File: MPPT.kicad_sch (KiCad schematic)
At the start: 95 parts

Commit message: schematic and layout revision.
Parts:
- removed C? (x2): 100uF, Capacitor_SMD:C_1210_3225Metric, symbol Device:C
- removed C?: 47uF, Capacitor_SMD:C_1206_3216Metric, symbol Device:C
- removed C?: 10uF, Capacitor_SMD:C_0805_2012Metric, symbol Device:C_Small
- removed C? (x2): 100nF, Capacitor_SMD:C_0805_2012Metric, symbol Device:C_Small
- removed D? (x3): 3.9V Zener, Diode_SMD:D_SOD-123F, symbol Device:D_Zener_Small
- removed D?: Diode, Diode_SMD:D_SOD-123F, symbol Device:D_Small
- removed L?: 6.8uH, Inductor_SMD:L_Taiyo-Yuden_NR-50xx, symbol Device:L_Small
- removed LED?: Tracking (Blue), LED_SMD:LED_0805_2012Metric, symbol Device:LED_Small
- removed LED?: Array Live (Green), LED_SMD:LED_0805_2012Metric, symbol Device:LED_Small
- removed LED?: Battery Live (Green), LED_SMD:LED_0805_2012Metric, symbol Device:LED_Small
- removed LED?: PWM (Blue), LED_SMD:LED_0805_2012Metric, symbol Device:LED_Small
- removed LED?: Car 12V (Green), LED_SMD:LED_0805_2012Metric, symbol Device:LED_Small
- removed LED?: Device 9V (Green), LED_SMD:LED_0805_2012Metric, symbol Device:LED_Small
- removed LED?: CAN_Tx (Blue), LED_SMD:LED_0805_2012Metric, symbol Device:LED_Small
- removed LED?: CAN_Rx (Blue), LED_SMD:LED_0805_2012Metric, symbol Device:LED_Small
- removed LED?: BPS Full (Blue), LED_SMD:LED_0805_2012Metric, symbol Device:LED_Small
- removed LED?: Error (Amber), LED_SMD:LED_0805_2012Metric, symbol Device:LED_Small
- removed R? (x2): 2k, Resistor_SMD:R_0805_2012Metric, symbol Device:R
- removed R? (x2): 1k, Resistor_SMD:R_0805_2012Metric, symbol Device:R
- removed R? (x6): 330, Resistor_SMD:R_0805_2012Metric, symbol Device:R
- removed R?: 15k, Resistor_SMD:R_0805_2012Metric, symbol Device:R
- removed R? (x2): 100k, Resistor_SMD:R_0805_2012Metric, symbol Device:R
- removed R?: 27k, Resistor_SMD:R_0805_2012Metric, symbol Device:R
- removed TP?: Arr_V, TestPoint:TestPoint_Pad_1.0x1.0mm, symbol Connector:TestPoint
- removed TP?: -ARR, TestPoint:TestPoint_Pad_1.0x1.0mm, symbol Connector:TestPoint
- removed TP?: +ARR, TestPoint:TestPoint_Pad_1.0x1.0mm, symbol Connector:TestPoint
- removed TP?: +BATT, TestPoint:TestPoint_Pad_1.0x1.0mm, symbol Connector:TestPoint
- removed TP?: -BATT, TestPoint:TestPoint_Pad_1.0x1.0mm, symbol Connector:TestPoint
- removed TP?: Board GND, TestPoint:TestPoint_Pad_1.0x1.0mm, symbol Connector:TestPoint
- removed TP?: Batt_V, TestPoint:TestPoint_Pad_1.0x1.0mm, symbol Connector:TestPoint
- removed TP?: Car GND, TestPoint:TestPoint_Pad_1.0x1.0mm, symbol Connector:TestPoint
- removed TP?: 12V, TestPoint:TestPoint_Pad_1.0x1.0mm, symbol Connector:TestPoint
- removed TP?: +5V, TestPoint:TestPoint_Pad_1.0x1.0mm, symbol Connector:TestPoint
- removed U?: PQMC3-D12-S9-S, MPPT-PrimaryPCB:490_PQMC3_D12_S12_S, symbol Array:PWR_REG_PQMC3-Dx-Sx-S
- removed U? (x2): MAX40075, Package_TO_SOT_SMD:SOT-23-6, symbol Amplifier_Operational:MAX4238AUT
- added C1, C14, C19, C2: 10uF, Capacitor_SMD:C_0805_2012Metric, symbol Device:C_Small
- added C10, C11, C12, C13, C15, C16, C20: 100nF, Capacitor_SMD:C_0805_2012Metric, symbol Device:C_Small
- added C17, C21: 10nF, Capacitor_SMD:C_0805_2012Metric, symbol Device:C_Small
- added C18: 220nF, Capacitor_SMD:C_0805_2012Metric, symbol Device:C_Small
- added D1: 13.2V, Diode_SMD:D_SOD-323F, symbol Device:D_Zener_Small
- added D10, D2, D7, D8, D9: 3.3V Zener, Diode_SMD:D_MiniMELF, symbol Device:D_Zener_Small
- added J5: CAN_In, Connector_Molex:Molex_Micro-Fit_3.0_43650-0415_1x04_P3.00mm_Vertical, symbol MPPT:CAN_Connector_43650-0427
- added J6: CAN_Out, Connector_Molex:Molex_Micro-Fit_3.0_43650-0415_1x04_P3.00mm_Vertical, symbol MPPT:CAN_Connector_43650-0427
- added JP1: Jumper, Connector_PinHeader_2.54mm:PinHeader_1x02_P2.54mm_Vertical, symbol Jumper:Jumper_2_Bridged
- added L3, L4: 1.8kOhm, Inductor_SMD:L_0805_2012Metric, symbol Device:FerriteBead_Small
- added LED1: 5V (Green), LED_SMD:LED_0805_2012Metric, symbol Device:LED_Small
- added LED10: Error (Amber), LED_SMD:LED_0805_2012Metric, symbol Device:LED
- added LED3, LED4: 9V (Green), LED_SMD:LED_0805_2012Metric, symbol Device:LED
- added LED5: Heartbeat (Blue), LED_SMD:LED_0805_2012Metric, symbol Device:LED
- added LED6: Tracking (Blue), LED_SMD:LED_0805_2012Metric, symbol Device:LED
- added LED7: PWM (Blue), LED_SMD:LED_0805_2012Metric, symbol Device:LED
- added LED8: CAN_Rx (Blue), LED_SMD:LED_0805_2012Metric, symbol Device:LED
- added LED9: CAN_Tx (Blue), LED_SMD:LED_0805_2012Metric, symbol Device:LED
- added R1: 330, Resistor_SMD:R_0805_2012Metric, symbol Device:R_Small
- added R10, R8: 100k, Resistor_SMD:R_0805_2012Metric, symbol Device:R
- added R11: 2k, Resistor_SMD:R_0805_2012Metric, symbol Device:R
- added R12: 0, Resistor_SMD:R_0805_2012Metric, symbol Device:R
- added R13, R14: 60.4, Resistor_SMD:R_0805_2012Metric, symbol Device:R_Small
- added R15: 15k, Resistor_SMD:R_0805_2012Metric, symbol Device:R
- added R16: 27k, Resistor_SMD:R_0805_2012Metric, symbol Device:R
- added R17, R18, R19, R20, R21, R22: 330, Resistor_SMD:R_0805_2012Metric, symbol Device:R
- added R6, R7: 2m, Resistor_SMD:R_1206_3216Metric, symbol Device:R
- added R9: 3k, Resistor_SMD:R_0805_2012Metric, symbol Device:R
- added TP1: 12V, TestPoint:TestPoint_Pad_1.0x1.0mm, symbol Connector:TestPoint
- added TP14, TP18: GND, TestPoint:TestPoint_Pad_1.0x1.0mm, symbol Connector:TestPoint
- added TP15: -ARR, TestPoint:TestPoint_Pad_1.0x1.0mm, symbol Connector:TestPoint
- added TP16: Array Current, TestPoint:TestPoint_Pad_1.0x1.0mm, symbol Connector:TestPoint
- added TP17: -BATT, TestPoint:TestPoint_Pad_1.0x1.0mm, symbol Connector:TestPoint
- added TP19: Battery Current, TestPoint:TestPoint_Pad_1.0x1.0mm, symbol Connector:TestPoint
- added TP2: Car GND, TestPoint:TestPoint_Pad_1.0x1.0mm, symbol Connector:TestPoint
- added TP20: +ARR, TestPoint:TestPoint_Pad_1.0x1.0mm, symbol Connector:TestPoint
- added TP21: Arr_V, TestPoint:TestPoint_Pad_1.0x1.0mm, symbol Connector:TestPoint
- added TP22: +BATT, TestPoint:TestPoint_Pad_1.0x1.0mm, symbol Connector:TestPoint
- added TP23: Batt_V, TestPoint:TestPoint_Pad_1.0x1.0mm, symbol Connector:TestPoint
- added TP24: CAN_Tx, TestPoint:TestPoint_Pad_1.0x1.0mm, symbol Connector:TestPoint
- added TP25: CAN_Rx, TestPoint:TestPoint_Pad_1.0x1.0mm, symbol Connector:TestPoint
- added TP26: CAN_ISO_Vout, TestPoint:TestPoint_Pad_1.0x1.0mm, symbol Connector:TestPoint
- added TP27: CAN_ISO_Vin, TestPoint:TestPoint_Pad_1.0x1.0mm, symbol Connector:TestPoint
- added TP28: CAN_ISO_GndIn, TestPoint:TestPoint_Pad_1.0x1.0mm, symbol Connector:TestPoint
- added TP29: CAN_ISO_GndOut, TestPoint:TestPoint_Pad_1.0x1.0mm, symbol Connector:TestPoint
- added TP3: +9V, TestPoint:TestPoint_Pad_1.0x1.0mm, symbol Connector:TestPoint
- added TP30: CAN_H, TestPoint:TestPoint_Pad_1.0x1.0mm, symbol Connector:TestPoint
- added TP31: CAN_L, TestPoint:TestPoint_Pad_1.0x1.0mm, symbol Connector:TestPoint
- added TP4: +3V3, TestPoint:TestPoint_Pad_1.0x1.0mm, symbol Connector:TestPoint
- added TP5: +5V, TestPoint:TestPoint_Pad_1.0x1.0mm, symbol Connector:TestPoint
- added TP6: Board GND, TestPoint:TestPoint_Pad_1.0x1.0mm, symbol Connector:TestPoint
- added U1: RI3-1205S, MPPT:CONV_RI3-1205S, symbol MPPT:RI3-1205S
- added U10: CDSOT23-T24CAN, Package_TO_SOT_SMD:SOT-23, symbol MPPT:CAN_Bus_Protector_CDSOT23-T24CAN
- added U5, U6: INA210, Package_DFN_QFN:UQFN-10_1.4x1.8mm_P0.4mm, symbol MPPT:OP_AMP_INA21x
- added U7, U8: MAX40075, Package_TO_SOT_SMD:SOT-23-6, symbol Amplifier_Operational:MAX4238AUT
- added U9: ADM3055E, MPPT:ADM3055EBRIZ, symbol MPPT:CAN_Chip_ADM3055E
- C3, C4: renamed from C?; Manufacturer Samsung Electro-Mechanics -> Samsung Elctro-Mechanics; Manufacturer Part Number (none) -> CL21B104KCFNNNE; Mouser Part (none) -> N/A; Part Number N/A -> (none); Projected Cost 0.0079 -> 0.0083
- C5: renamed from C?; Manufacturer Part Number (none) -> CL21B105KBFNNNE; Mouser Part (none) -> N/A; Part Number N/A -> (none)
- C6, C7: renamed from C?; Manufacturer Part Number (none) -> CL21A475KAQNNNE; Mouser Part (none) -> N/A; Part Number N/A -> (none)
- C8: renamed from C?; Manufacturer Part Number (none) -> 0805F225M500NT; Mouser Part (none) -> N/A; Part Number N/A -> (none)
- C9: renamed from C?; Alternative See 1nF, 2.2nF, 4.7nF, 10nF, 22nF, 47nF versions. -> (none); Alternative Part (none) -> See 1nF, 2.2nF, 4.7nF, 10nF, 22nF, 47nF versions.; Manufacturer Part Number (none) -> MKT1813247635; Mouser Part (none) -> 75-MKT1813247635; Part Number 75-MKT1813247635 -> (none)
- CP1, CP2: renamed from CP?; Manufacturer Part Number (none) -> SLPX102M250E5P3; Mouser Part (none) -> 598-SLPX102M250E5P3; Part Number 598-SLPX102M250E5P3 -> (none)
- D3: renamed from D?; Manufacturer Part Number (none) -> BZT52H-B16,115; Mouser Part (none) -> 771-BZT52HB16115; Part Number 771-BZT52HB16115 -> (none)
- D4, D5, D6: renamed from D?; Manufacturer Part Number (none) -> SCS308AHGC9; Mouser Part (none) -> 755-SCS308AHGC9; Part Number 755-SCS308AHGC9 -> (none)
- F1, F2: renamed from F?; footprint IV Curve Tracer:05200101Z_Fuze_Holder_5x20_PCB_Mount -> MPPT:05200101Z_Fuze_Holder_5x20_PCB_Mount; Manufacturer Part Number (none) -> 05200101Z; Mouser Part (none) -> 576-05200101Z; Part Number 576-05200101Z -> (none)
- HS1, HS2, HS3: renamed from HS?; Manufacturer Part Number (none) -> FA-T220-38E; Mouser Part (none) -> 588-FA-T220-38E; Part Number 588-FA-T220-38E -> (none)
- J1: renamed from J?; symbol Array:PWR_Connector_43650-0215 -> MPPT:PWR_Connector_43650-0215; Manufacturer Part Number (none) -> 43650-0215; Mouser Part (none) -> 538-43650-0215; Part Number 538-43650-0215 -> (none)
- J2: renamed from J?; Manufacturer Part Number (none) -> 43650-0215; Mouser Part (none) -> 538-43650-0215; Part Number 538-43650-0215 -> (none)
- J3, J4: renamed from J?; footprint IV Curve Tracer:PhoenixContact_PowerCombicon5_GF_2x7.62mm -> MPPT:PhoenixContact_PowerCombicon5_GF_2x7.62mm; symbol Array:PWR_Connector_1720796 -> MPPT:PWR_Connector_1720796; Manufacturer Part Number (none) -> 1720796; Mouser Part (none) -> 651-1720796; Part Number 651-1720796 -> (none)
- L1: renamed from L?; Manufacturer Part Number (none) -> NRS5040T6R8MMGJ; Mouser Part (none) -> 963-NRS5040T6R8MMGJ; Part Number 963-NRS5040T6R8MMGJ -> (none)
- L2: renamed from L?; footprint MPPT-PrimaryPCB:L_Toroid_Vertical_L46.0mm_W19.1mm_P21.80mm_Bourns_5700 -> MPPT:L_Toroid_Vertical_L46.0mm_W19.1mm_P21.80mm_Bourns_5700; Manufacturer Part Number (none) -> HF400-601M-8.0AV; Mouser Part (none) -> N/A; Part Number HF400-601M-8.0AV -> (none)
- LED2: renamed from LED?; Manufacturer Part Number (none) -> APTD2012LCGCK; Mouser Part (none) -> 604-APTD2012LCGCK; Part Number 604-APTD2012LCGCK -> (none)
- Q1, Q2: renamed from Q?; Alternative Part (none) -> https://www.mouser.com/ProductDetail/IXYS/IXTH62N65X2?qs=uw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; Manufacturer Toshiba -> IXYS; Manufacturer Part Number (none) -> IXFH80N65X2; Mouser Part (none) -> 747-IXFH80N65X2; Part Number 757-TK040N65ZS1F -> (none); Purchase Page https://www.mouser.com/ProductDetail/Toshiba/TK040N65ZS1F?q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 -> https://www.mouser.com/ProductDetail/IXYS/IXFH80N65X2?qs=gQ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
- R2: renamed from R?; Manufacturer Part Number (none) -> CRCW08051R50FKEAHP; Mouser Part (none) -> 71-CRCW08051R50FKEAH; Part Number 71-CRCW08051R50FKEAH -> (none)
- R3: renamed from R?; Manufacturer Part Number (none) -> 0805W8F3300T5E; Mouser Part (none) -> N/A; Part Number N/A -> (none)
- R4: renamed from R?; Manufacturer Part Number (none) -> 0805W8F1002T5E; Mouser Part (none) -> N/A; Part Number N/A -> (none)
- R5: renamed from R?; Alternative See 2, 10, 20, 33, 75, 150 ohm versions. -> (none); Alternative Part (none) -> See 2, 10, 20, 33, 75, 150 ohm versions.; Manufacturer Part Number (none) -> PWR220T-35-33R0J; Mouser Part (none) -> 652-PWR220T-35-33R0J; Part Number 652-PWR220T-35-33R0J -> (none)
- SW1: renamed from SW?; Manufacturer Part Number (none) -> TS02-66-50-BK-260-SCR-D; Mouser Part (none) -> 179-TS026650BK260SCR; Part Number 179-TS026650BK260SCR -> (none)
- SW2: renamed from SW?; footprint MPPT-PrimaryPCB:ADF02ST04_DIP_Switch_2_POS -> MPPT:ADF02ST04_DIP_Switch_2_POS; Manufacturer Part Number (none) -> ADF02ST04; Mouser Part (none) -> 506-ADF02ST04; Part Number 506-ADF02ST04 -> (none)
- U2: renamed from U?; footprint IV Curve Tracer:MODULE_NUCLEO-L432KC -> MPPT:MODULE_NUCLEO-L432KC; symbol Array:MCU_Nucleo_L432KC -> MPPT:MCU_Nucleo_L432KC; Manufacturer Part Number (none) -> 511-NUCLEO-L432KC; Mouser Part (none) -> 511-NUCLEO-L432KC; Part Number 511-NUCLEO-L432KC -> (none)
- U3: renamed from U?; symbol Array:UCC37321 -> MPPT:UCC37321; Manufacturer Part Number (none) -> UCC37321D; Mouser Part (none) -> N/A; Part Number UCC37321D -> (none)
- U4: renamed from U?; footprint IV Curve Tracer:IES01_PDS1 -> MPPT:IES01_PDS1; symbol Array:IES01_PDS1 -> MPPT:IES01_PDS1; Manufacturer Part Number (none) -> IES0105S09; Mouser Part (none) -> 209-IES0105S09; Part Number 209-IES0105S09 -> (none)
- gave numbers to parts that had none: 11
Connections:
- net +12V: now also C1.1, D1.1 (K), TP1.1, U1.2 (+VIN)
- net +3V3: now also C16.2, C17.1, TP4.1, U9.4 (V_IO)
- net +5V: now also C14.1, C15.2, C2.1, R1.1, TP5.1, U1.4 (+VOUT), U9.3 (V_In)
- net +9V: now also J2.1 (Pin_1), TP3.1; no longer J2.2 (Pin_2)
- net +9VA: now also C10.2, C11.2, C12.2, C13.2, U5.3 (V+), U6.3 (V+), U7.6 (V+), U8.6 (V+)
- net Array_Current: now also D7.1 (K), TP16.1, U5.6
- net Array_Voltage: now also D9.1 (K), TP21.1, U7.1, U7.4 (-)
- net Battery_Current: now also D8.1 (K), TP19.1, U6.6
- net Battery_Voltage: now also D10.1 (K), TP23.1, U8.1, U8.4 (-)
- net CAN_Rx: now also R20.1, TP25.1, U9.5 (RX)
- net CAN_Tx: now also R21.1, TP24.1, U9.7 (TX)
- net Error: now also R22.1
- net GND: now also J2.2 (Pin_2), C10.1, C11.1, C12.1, C13.1, C14.2, C15.1, C16.1, C17.2, C2.2, D10.2 (A), D2.2 (A), D7.2 (A), D8.2 (A), D9.2 (A), LED1.1 (K), LED10.1 (K), LED5.1 (K), LED6.1 (K), LED7.1 (K), LED8.1 (K), LED9.1 (K), R11.2, R6.2, R7.1, R9.2, TP14.1, TP18.1, TP6.1, U1.3 (-VOUT), U5.1 (REF), U5.2 (V-), U5.4 (+), U6.1 (REF), U6.2 (V-), U6.5 (-), U7.2 (V-), U7.5 (~{SHDN}), U8.2 (V-), U8.5 (~{SHDN}), U9.1 (GND_In), U9.10 (GND_In), U9.2 (GND_In); no longer J2.1 (Pin_1)
- net GNDPWR: now also C1.2, D1.2 (A), TP2.1, U1.1 (-VIN)
- net Heartbeat: now also R17.1
- net PWM: now also D2.1 (K), R19.1
- net Tracking: now also R18.1
- net +ARR: now reaches CP1.1, F1.1, L2.1
- net +ARR: now also R15.1, R8.2, TP20.1
- net +BATT: now reaches CP2.1, D5.1 (K), D6.1 (K), F2.2
- net +BATT: now also R10.2, R16.1, TP22.1
- net -Arr renamed -ARR
- net -ARR: now also LED3.1 (K), R6.1, TP15.1, U5.5 (-)
- net -Batt renamed -BATT
- net -BATT: now also LED4.1 (K), R7.2, TP17.1, U6.4 (+)
- net BPS_Full: no longer names the net of U2.12 (D9)
- new net: R8.1, R9.1, U7.3 (+)
- new net: LED1.2 (A), R1.2
- new net: C19.2, C20.1, C21.2, J5.2 (GND), J6.2 (GND), L4.1, R12.2, TP28.1, U10.3 (GND), U9.11 (GND_ISO_In), U9.15 (GND_ISO_In)
- new net: C18.2, L4.2, TP29.1, U9.18 (GND_ISO_Out), U9.20 (GND_ISO_Out)
- new net: LED4.2 (A), R16.2
- new net: LED5.2 (A), R17.2
- new net: R12.1, U9.12 (RS)
- new net: J5.4 (CAN_L), J6.4 (CAN_L), R14.2, TP31.1, U10.2 (CAN_L), U9.13 (CAN_L)
- new net: J5.3 (CAN_H), J6.3 (CAN_H), R13.1, TP30.1, U10.1 (CAN_H), U9.14 (CAN_H)
- new net: C19.1, C20.2, C21.1, J5.1 (5V), J6.1 (5V), L3.1, TP27.1, U9.16 (V_ISO_In)
- new net: C18.1, L3.2, TP26.1, U9.19 (V_ISO_Out)
- new net: LED8.2 (A), R20.2
- new net: LED3.2 (A), R15.2
- new net: LED9.2 (A), R21.2
- new net: R10.1, R11.1, U8.3 (+)
- new net: JP1.1 (A), R13.2
- new net: JP1.2 (B), R14.1
- new net: LED6.2 (A), R18.2
- new net: LED10.2 (A), R22.2
- new net: LED7.2 (A), R19.2
- no-connect marks 11 -> 15
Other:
- note added: "0-100V"
- note added: "0-150V"
- note added: "0-3V"
- note added: "0-6A"
- note added: "0-8A"
- note added: "7.5A 0-15mV"
- note added: "CAN"
- note added: "CAN Bus Protection"
- note added: "HIGH CURRENT FLOWS THROUGH THIS LOOP."
- note added: "Inputs: -10.8-13.2VDC (Car Power) -7-12VDC (External 9V Supply) -5VDC (Nucleo USB)"
- note added: "Must be close to V_ISO_In"
- note added: "Must be close to V_ISO_Out"
- note added: "Nucleo Connections"
- note added: "PWM Gate Driver"
- note added: "Powered and controlled by USB through STLink UART. Requires A7 (PA2) and A2 (PA3) to be reserved."
- note added: "VIN: 7-12V -> Input 5V0: 5V -> Output on USB/VIN 3V3: 3.3V -> Output always"
- note removed: "For decoupling, we add extra capacitors and unlink the power pins on either side."
- note removed: "GNDPWR"
- note removed: "High Power Control"
- note removed: "NOTE: We would ordinarily isolate the Nucleo from the high power regions, but we don't have a good way to do that without redesigning our sensors and our software. Therefore, for reasons of expediency, we're placing the Nucleo on the high power plane."
- note removed: "Note that A7 (PA2) and A2 (PA3) are reserved for STLink UART."
- moved on the sheet: C3, C4, C5, C6, C7, C8, C9, CP1, CP2, D3, D4, D5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

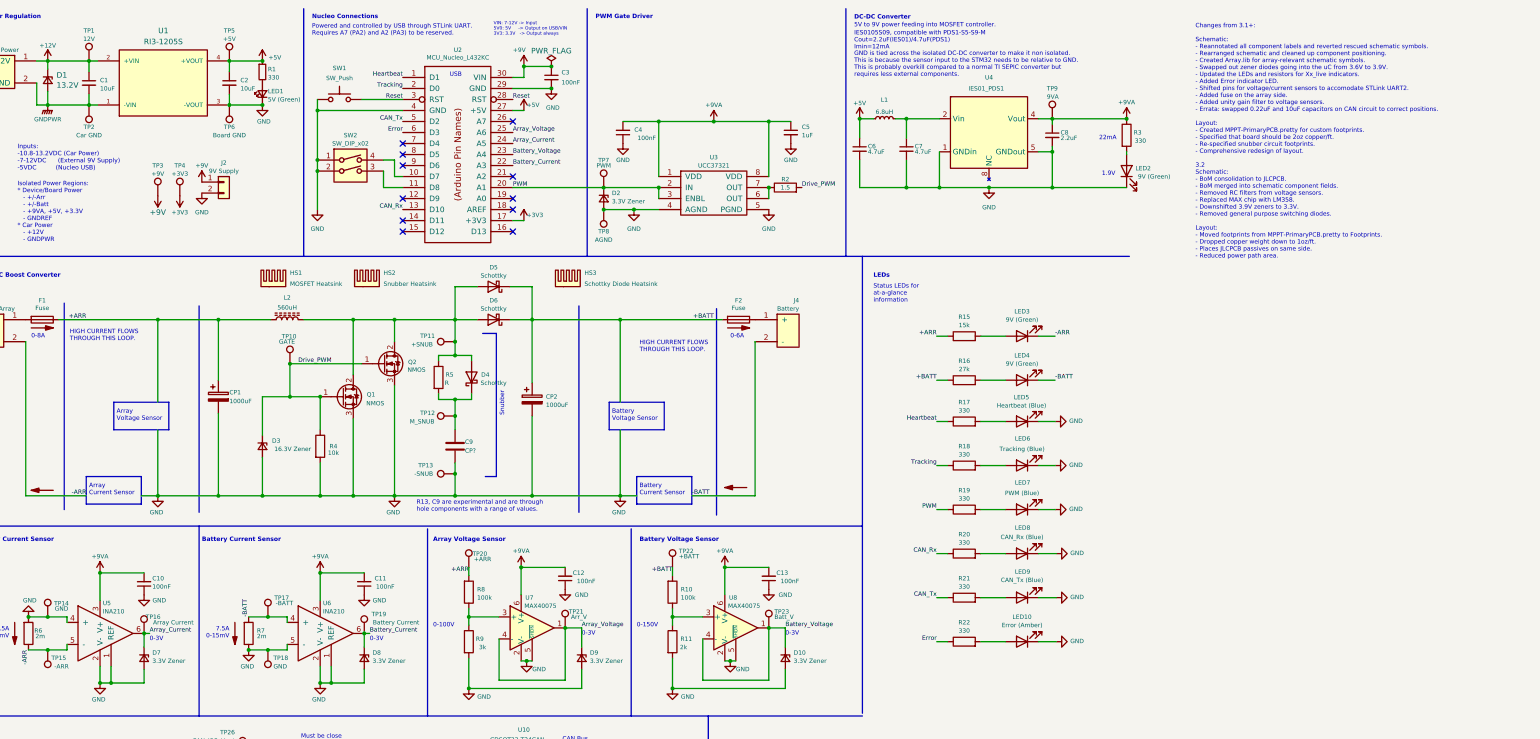
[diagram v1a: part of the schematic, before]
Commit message: Revisions on schematic and layout. See notes in the schematic for changes.
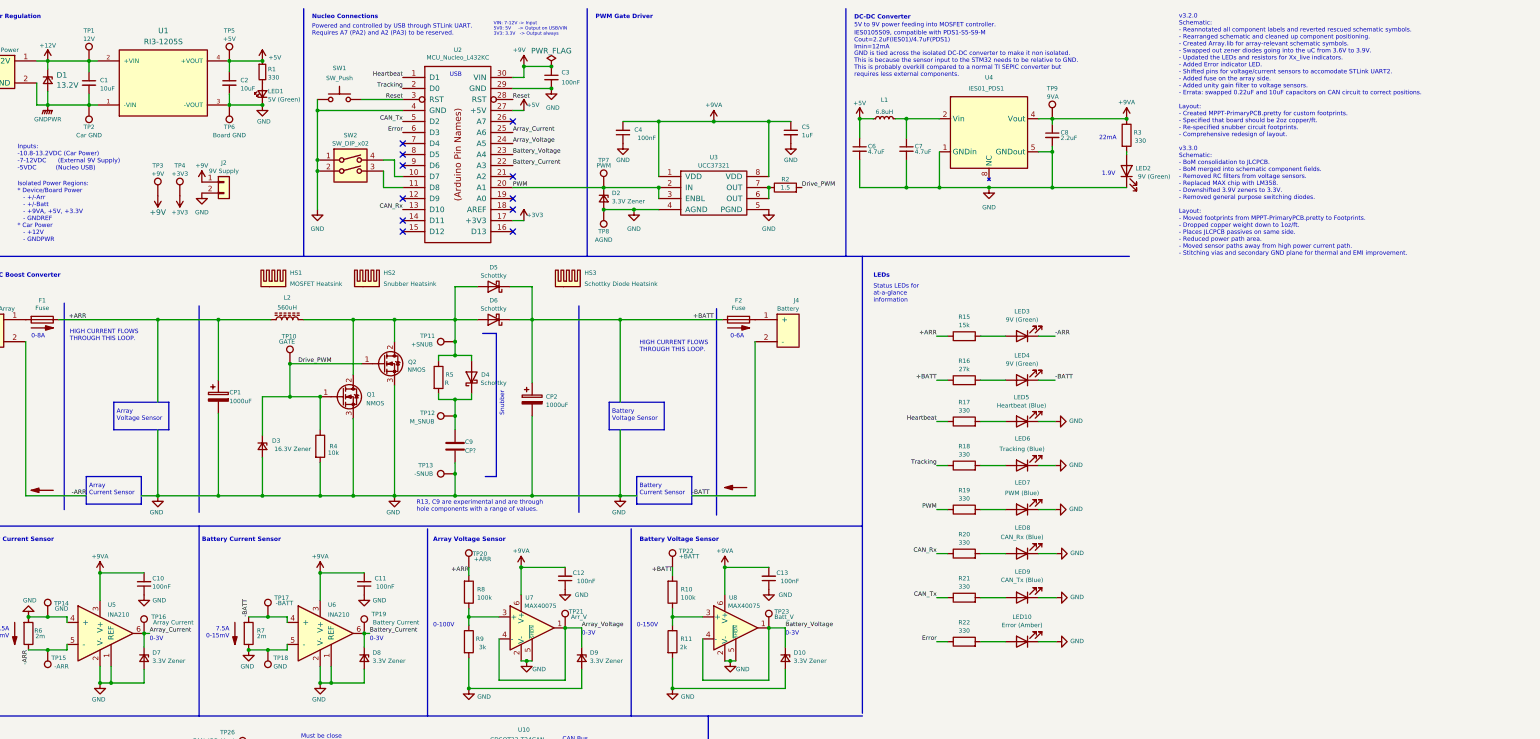
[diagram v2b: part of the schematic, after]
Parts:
- removed U5, U6: INA210, Package_DFN_QFN:UQFN-10_1.4x1.8mm_P0.4mm, symbol MPPT:OP_AMP_INA21x
- added U5, U6: INA210, Package_TO_SOT_SMD:SOT-363_SC-70-6_Handsoldering, symbol Array:OP_AMP_INA21x
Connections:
- net +9VA: now also U5.3 (V+), U6.3 (V+)
- net -ARR: now also U5.5 (-)
- net -BATT: now also U6.4 (+)
- net Array_Current: now also U2.25 (A6), U5.6; no longer U2.24 (A5)
- net Array_Voltage: now also U2.24 (A5); no longer U2.25 (A6)
- net Battery_Current: now also U6.6
- net GND: now also U5.1 (REF), U5.2 (V-), U5.4 (+), U6.1 (REF), U6.2 (V-), U6.5 (-)
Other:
- note added: "v3.2.0 Schematic: - Reannotated all component labels and reverted rescued schematic symbols. - Rearranged schematic and cleaned up component positioning. - Created Array.lib for array-relevant schematic symbols. - Swapped out zener diodes going into the uC from 3.6V to 3.9V. - Updated the LEDs and resistors for Xx_live indicators. - Added Error indicator LED. - Shifted pins for voltage/current se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"
- note removed: "Changes from 3.1+: Schematic: - Reannotated all component labels and reverted rescued schematic symbols. - Rearranged schematic and cleaned up component positioning. - Created Array.lib for array-relevant schematic symbols. - Swapped out zener diodes going into the uC from 3.6V to 3.9V. - Updated the LEDs and resistors for Xx_live indicators. - Added Error indicator LED. - Shifted pins for voltag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"

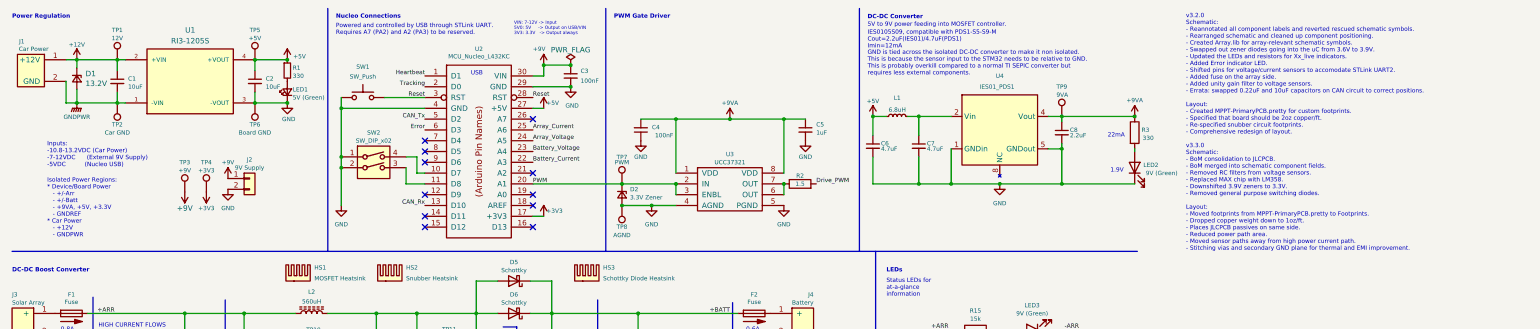
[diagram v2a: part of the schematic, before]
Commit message: gerber rebuild for JLPCB errors
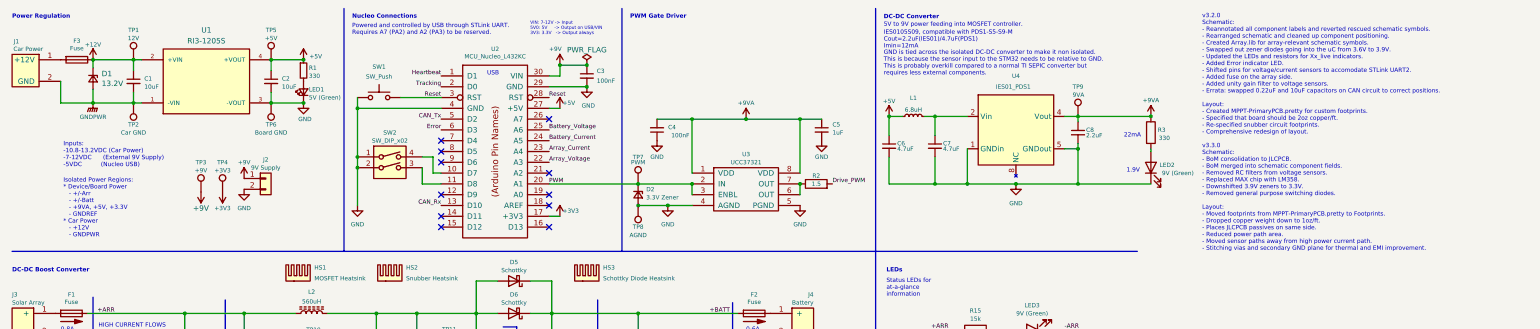
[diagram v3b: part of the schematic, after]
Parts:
- added F3: Fuse, Footprints:05200101Z_Fuze_Holder_5x20_PCB_Mount, symbol Device:Fuse
- F1, F2: footprint MPPT:05200101Z_Fuze_Holder_5x20_PCB_Mount -> Footprints:05200101Z_Fuze_Holder_5x20_PCB_Mount
- J3, J4: footprint MPPT:PhoenixContact_PowerCombicon5_GF_2x7.62mm -> Footprints:PhoenixContact_PowerCombicon5_GF_2x7.62mm
- L2: footprint MPPT:L_Toroid_Vertical_L46.0mm_W19.1mm_P21.80mm_Bourns_5700 -> Footprints:L_Toroid_Vertical_L46.0mm_W19.1mm_P21.80mm_Bourns_5700
- SW2: footprint MPPT:ADF02ST04_DIP_Switch_2_POS -> Footprints:ADF02ST04_DIP_Switch_2_POS
- U1: footprint MPPT:CONV_RI3-1205S -> Footprints:CONV_RI3-1205S
- U2: footprint MPPT:MODULE_NUCLEO-L432KC -> Footprints:MODULE_NUCLEO-L432KC
- U4: footprint MPPT:IES01_PDS1 -> Footprints:IES01_PDS1
- U9: footprint MPPT:ADM3055EBRIZ -> Footprints:ADM3055EBRIZ
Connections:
- net +12V: now also F3.1; no longer J1.1 (+12V)
- net Array_Current: now also U2.23 (A4); no longer U2.25 (A6)
- net Array_Voltage: now also U2.22 (A3); no longer U2.24 (A5)
- net Battery_Current: now also U2.24 (A5); no longer U2.22 (A3)
- net Battery_Voltage: now also U2.25 (A6); no longer U2.23 (A4)
- new net: F3.2, J1.1 (+12V)
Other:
- moved on the sheet: C1, C2, C3, C4, C5, C6, C7, C8, D1, D2, J1, J2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

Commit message: v3.3.1 changes.
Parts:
- U4: Alternative Part https://www.mouser.com/ProductDetail/CUI-Inc/PDS1-S5-S9-M-T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 -> (none)
- U5, U6: symbol Array:OP_AMP_INA21x -> MPPT:OP_AMP_INA21x
- U7, U8: value MAX40075 -> OPA990; Manufacturer Maxim Integrated -> Texas Instruments; Manufacturer Part Number MAX40075AUT+ -> OPA990SIDBVR; Mouser Part 700-MAX40075AUT+ -> 595-OPA990SIDBVR; Projected Cost 2.13 -> 1.30; Purchase Page https://www.mouser.com/ProductDetail/Maxim-Integrated/MAX40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 -> https://www.mouser.com/ProductDetail/595-OPA990SIDBVR
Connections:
- net +9VA: now also U4.5 (Vout); no longer U4.4 (Vout)
- net GND: now also U4.4 (GNDout); no longer U4.5 (GNDout)
- net PWM: no longer U3.3 (ENBL)
- net PWM_EN: now reaches U2.19 (A0)
- net PWM_EN: now also U3.3 (ENBL)
- no-connect marks 15 -> 14
